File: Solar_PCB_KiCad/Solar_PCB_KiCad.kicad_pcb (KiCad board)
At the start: 2 copper layers, 70 x 39 mm, 23 parts, among them J1 Screw_Terminal_01x02, J2 Screw_Terminal_01x02, J3 Screw_Terminal_01x02, U1 LT3652EMSE

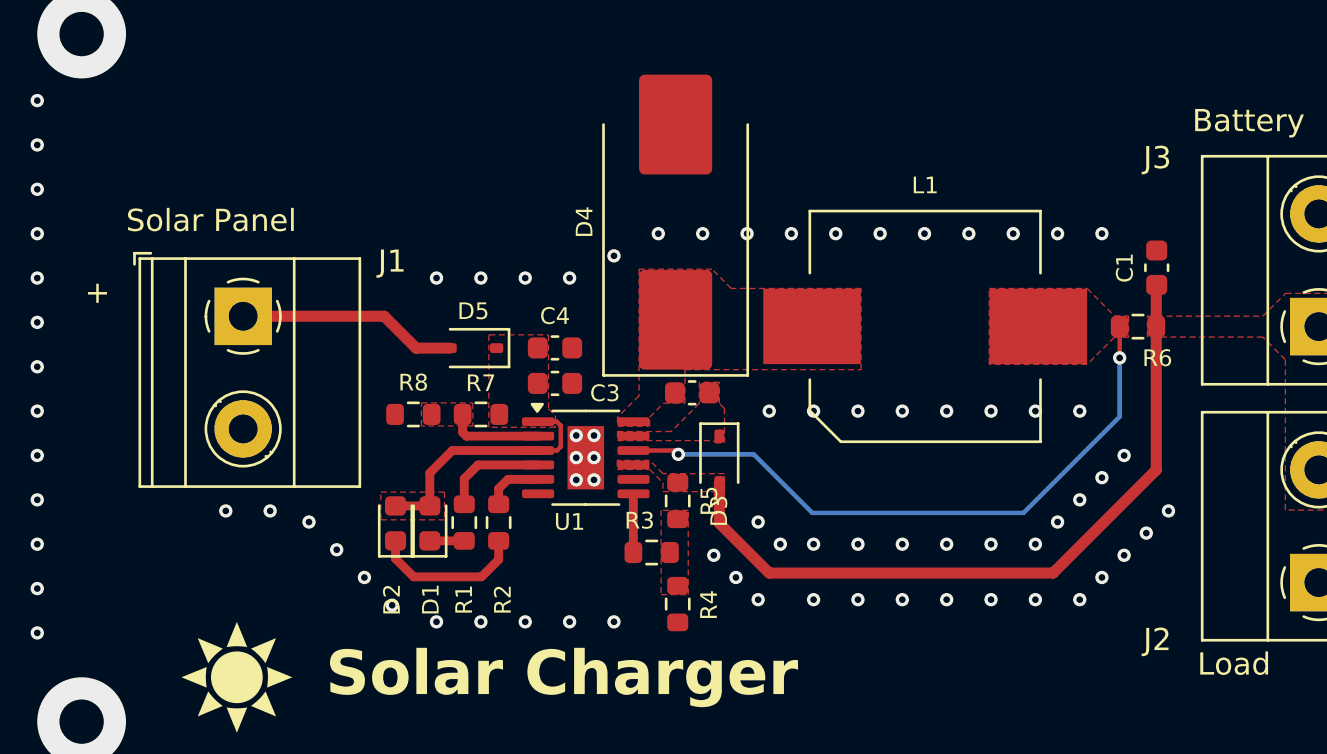
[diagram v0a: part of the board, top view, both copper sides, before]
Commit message: Added optional bypass and input capacitance
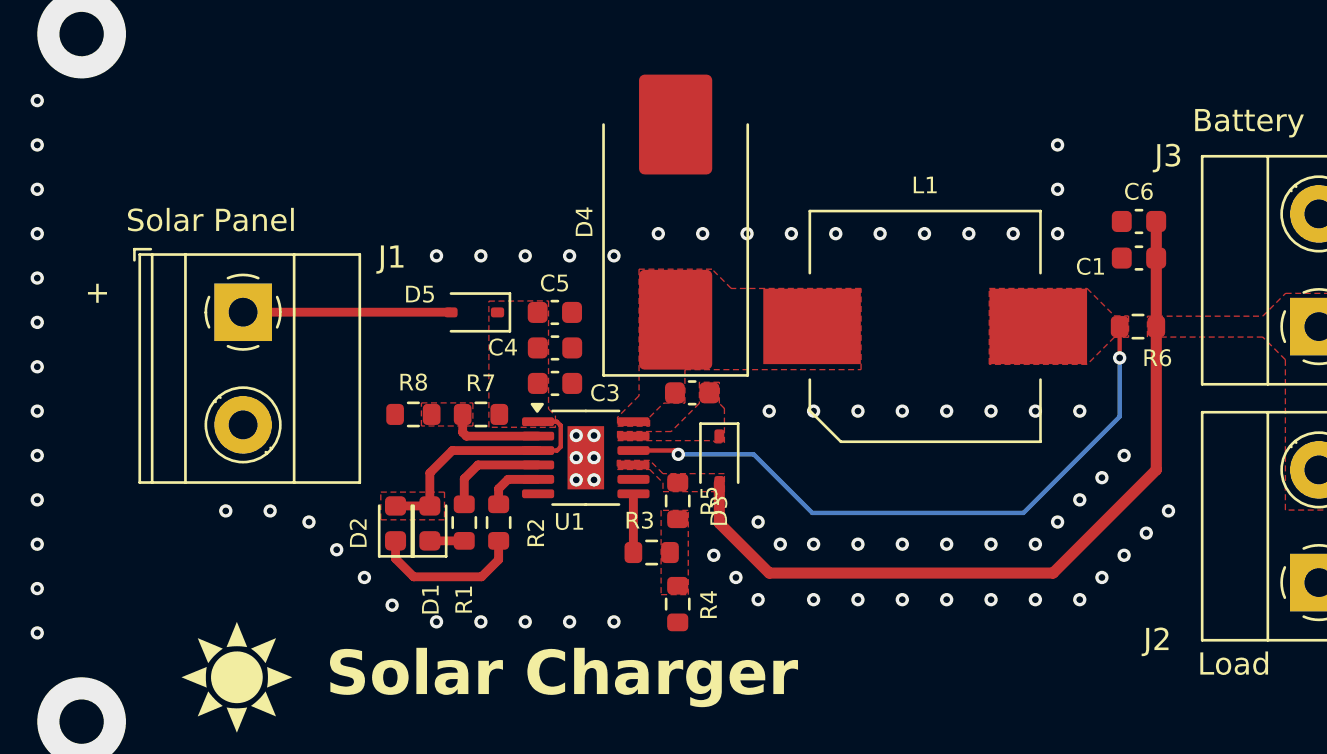
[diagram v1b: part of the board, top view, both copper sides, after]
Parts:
- added C5: 10u, Capacitor_SMD:C_0603_1608Metric, F.Cu at (146.3, 109.5)
- added C6: 100u, Capacitor_SMD:C_0603_1608Metric, F.Cu at (172.7, 105.5)
- moved D5 1.61 mm to (142.7, 109.5)
- moved C1 0.91 mm to (172.7, 107.1), turned to 180 degrees
- moved J1 0.18 mm to (132.3, 109.5)
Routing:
- net Net-(D3-A): track 32.7 -> 35.6 mm
- net Net-(D5-A): track 9.92 -> 9.37 mm
- net GND: vias 154 -> 156
- net (no net): vias 1 -> 0
